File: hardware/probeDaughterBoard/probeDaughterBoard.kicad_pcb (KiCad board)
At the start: 2 copper layers, 45 x 15 mm, 44 parts, among them J1 Conn_02x04_Odd_Even, J2 Conn_01x03_Socket, J3 Conn_01x02_Socket, J4 Conn_01x06

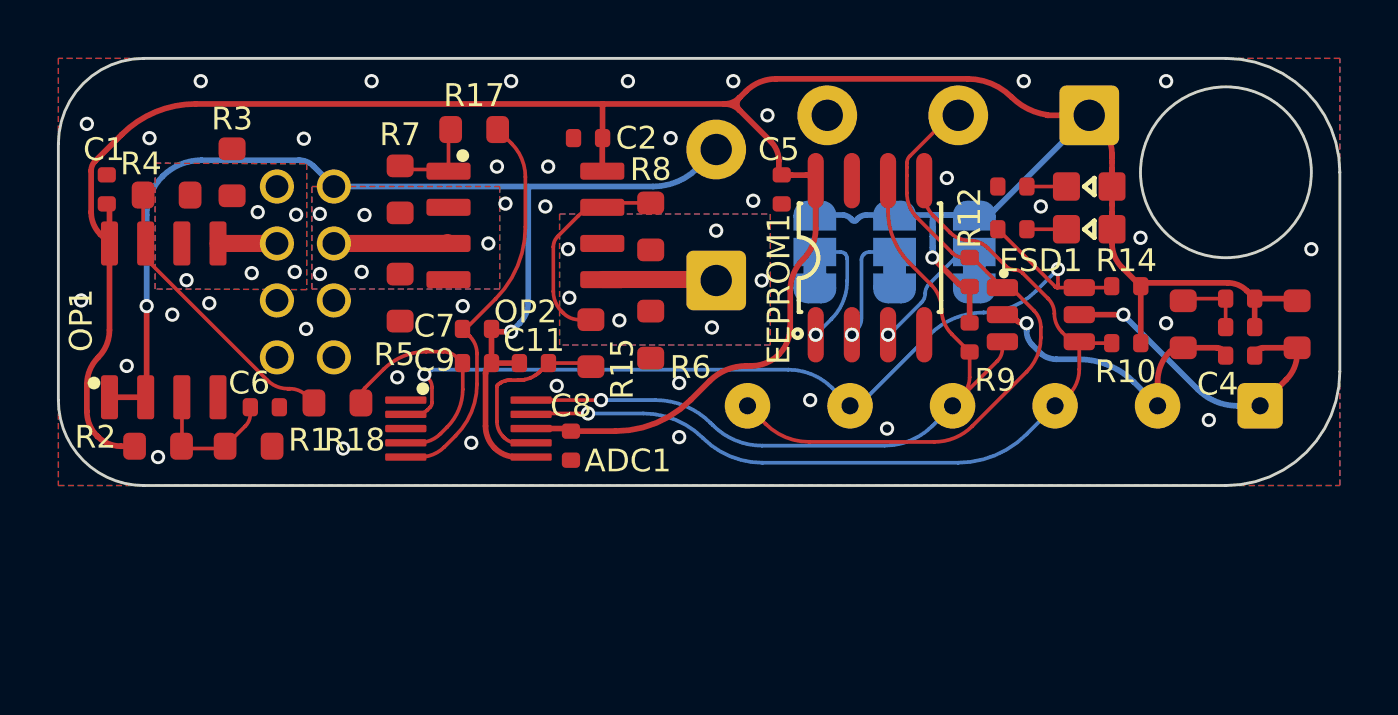
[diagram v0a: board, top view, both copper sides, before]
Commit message: -added CAD models -moved to KiCAD 8.0 -clang formatting -rebuild sensor calibration -add logging and analytics file -added adaptive backlight -added work hours for gps sync
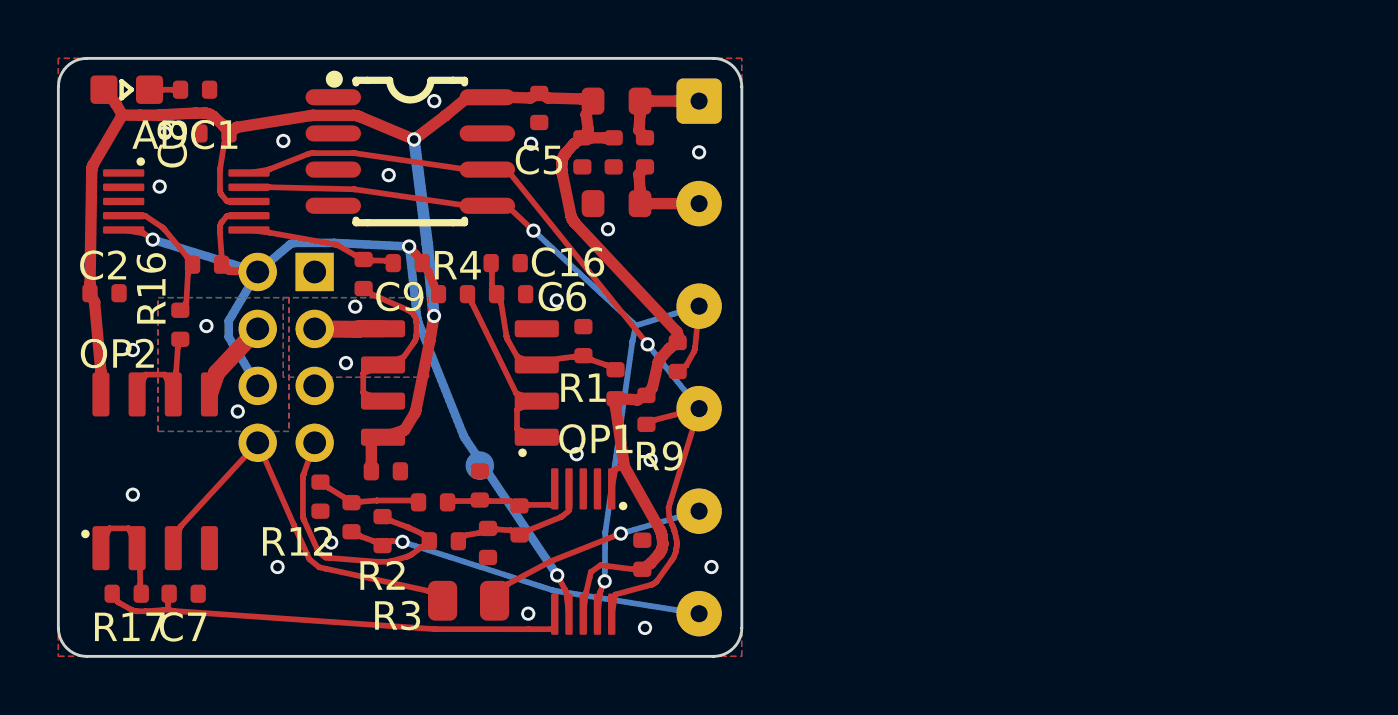
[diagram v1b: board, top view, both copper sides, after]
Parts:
- removed ESD1: SRV05, footprint:SOT-23-6_L2.9-W1.6-P0.95-LS2.8-BR
- removed J2: Conn_01x03_Socket, Connector_Wire:SolderWire-0.5sqmm_1x03_P4.6mm_D0.9mm_OD2.1mm
- removed J3: Conn_01x02_Socket, Connector_Wire:SolderWire-0.5sqmm_1x02_P4.6mm_D0.9mm_OD2.1mm
- removed JP1, JP2, JP3: SolderJumper_3_Bridged12, Jumper:SolderJumper-3_P1.3mm_Bridged12_RoundedPad1.0x1.5mm_NumberLabels
- removed LED2: 0603,Green, footprint:LED0603
- removed R18: 0603,100, footprint:0603_1608Metric
- removed R7, R8: 22k, footprint:0603_1608Metric
- added ADC2: ADS1015, footprint:MSOP-10_L3.0-W3.0-P0.50-LS5.0-BL, F.Cu at (18.4, 17.3)
- added C12: 0402,100nF,16V,X7R, footprint:0402_1005Metric, F.Cu at (20.5, 17.4)
- added C13: 0402,220nF,16V,X7R, footprint:0402_1005Metric, F.Cu at (16.2, 16.2)
- added C14: 0402,22nF,50V,X7R, footprint:0402_1005Metric, F.Cu at (14.8, 15.0)
- added C15: 0402,22nF,50V,X7R, footprint:0402_1005Metric, F.Cu at (15.1, 17.0)
- added C16: 0402,1uF,25V,X5R, footprint:0402_1005Metric, F.Cu at (15.7, 7.19)
- added R16: 0402,100, footprint:0402_1005Metric, F.Cu at (4.28, 9.35)
- added REF**: VREF, footprint:TestPoint_Pad_D1.0mm, B.Cu at (14.8, 14.3)
- R1: value 22k -> 0402,2.2k; footprint footprint:0603_1608Metric -> footprint:0402_1005Metric
- R12: value 0402,2.2k -> 0402,10k
- R13: value 0402,10k -> 0402,100
- R14: value 0402,4.7k -> 0402,100
- R15, R17: value 0603,100 -> 0402,100; footprint footprint:0603_1608Metric -> footprint:0402_1005Metric
- R2: value 22k -> 0402,10k; footprint footprint:0603_1608Metric -> footprint:0402_1005Metric
- R3: value 10k -> 0805,470k; footprint footprint:0603_1608Metric -> footprint:0805_2012Metric
- R4: value 22k -> 0402,100; footprint footprint:0603_1608Metric -> footprint:0402_1005Metric
- R5: value 10k -> 0402,47k; footprint footprint:0603_1608Metric -> footprint:0402_1005Metric
- R6: value 10k -> 0402,12k; footprint footprint:0603_1608Metric -> footprint:0402_1005Metric
- moved LED1 34.0 mm to (2.40, 1.10), turned to 180 degrees
- moved R11 25.9 mm to (10.3, 16.1), turned to 90 degrees
- moved R14 25.6 mm to (13.5, 17.0), turned to 0 degrees
- moved FB1 25.2 mm to (19.6, 1.50), turned to 0 degrees
- moved R12 24.1 mm to (9.20, 15.4), turned to -90 degrees
- moved C3 23.9 mm to (18.4, 3.30), turned to -90 degrees
- moved C10 22.6 mm to (19.5, 3.30), turned to -90 degrees
- moved R13 22.5 mm to (13.2, 15.6), turned to 0 degrees
- moved J4 22.4 mm to (22.5, 1.50), turned to -90 degrees
- moved C4 22.1 mm to (20.6, 3.30), turned to -90 degrees
- moved R17 20.4 mm to (2.40, 18.8)
- moved FB2 20.3 mm to (19.6, 5.10), turned to 0 degrees
- moved C2 17.8 mm to (1.62, 8.25), turned to 0 degrees
- moved R3 17.2 mm to (14.4, 19.0), turned to 180 degrees
- moved C8 16.6 mm to (5.48, 2.64), turned to 180 degrees
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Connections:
- ADC1 pad 1: unconnected-(ADC1-ADDR-Pad1) -> GND
- ADC1 pad 2: /INT -> unconnected-(ADC1-INT-Pad2)
- ADC1 pad 4: /PH_OUT -> /ORP_OUT
- ADC1 pad 5: /ORP_OUT -> /VREF
- ADC1 pad 6: /VREF -> /PH_OUT
- ADC1 pad 7: /NITRATE_OUT -> /VREF
- C11 pad 1: /NITRATE_OUT -> /ORP_OUT
- C6 pad 1: Net-(C6-Pad1) -> Net-(C16-Pad1)
- C7 pad 1: /ORP_OUT -> /EC_OUT
- C7 pad 2: /VREF -> GND
- EEPROM1 pad 1: Net-(EEPROM1-A0) -> GND
- EEPROM1 pad 2: Net-(EEPROM1-A1) -> GND
- EEPROM1 pad 3: Net-(EEPROM1-A2) -> GND
- J1 pad 1: /VREF -> unconnected-(J1-Pin_1-Pad1)
- J1 pad 2: unconnected-(J1-Pin_2-Pad2) -> /VREF
- J1 pad 3: /ORP_IN -> /PH_IN
- J1 pad 4: /PH_IN -> /ORP_IN
- J1 pad 5: /EC_INA -> GND
- J1 pad 6: /TEMP_INB -> /VREF
- J1 pad 7: /EC_INB -> /TEMP_IN
- J1 pad 8: /TEMP_INA -> /EC_IN
- J4 pad 5: /INT -> /EC_DRIVE
- J4 pad 6: /TEMP_OW -> /TEMP_DRIVE
- OP1 pad 1: /VREF -> Net-(OP1---Pad2)
- OP1 pad 2: /VREF -> Net-(OP1---Pad2)
- OP1 pad 3: Net-(C6-Pad1) -> Net-(C16-Pad1)
- OP1 pad 7: Net-(OP1-Pad7) -> /PH_RING
- OP2 pad 1: Net-(OP2-Pad1) -> Net-(OP2---Pad2)
- OP2 pad 2: /ORP_RING -> Net-(OP2---Pad2)
- OP2 pad 3: /ORP_IN -> /EC_IN
- OP2 pad 5: /NITRATE_IN -> /ORP_IN
- OP2 pad 6: /NITRATE_RING -> /ORP_RING
- OP2 pad 7: Net-(OP2-Pad7) -> /ORP_RING
- R1 pad 1: GND -> Net-(C16-Pad1)
- R1 pad 2: Net-(C6-Pad1) -> GND
- R11 pad 1: Net-(LED1-C) -> /TEMP_DRIVE
- R11 pad 2: GND -> /TEMP_REF
- R12 pad 1: +3.3V -> /TEMP_REF
- R12 pad 2: /TEMP_OW -> GND
- R13 pad 1: Net-(LED2-C) -> /TEMP_REF
- R13 pad 2: /INT -> Net-(ADC2-AIN1)
- R14 pad 1: +3.3V -> /TEMP_IN
- R14 pad 2: /INT -> Net-(ADC2-AIN0)
- R15 pad 1: /NITRATE_OUT -> /PH_RING
- R15 pad 2: Net-(OP2-Pad7) -> /PH_OUT
- R17 pad 1: /ORP_OUT -> Net-(OP2---Pad2)
- R17 pad 2: Net-(OP2-Pad1) -> /EC_OUT
- R2 pad 1: Net-(C6-Pad1) -> /TEMP_DRIVE
- R2 pad 2: +3.3V -> /TEMP_IN
- R3 pad 1: /PH_RING -> /EC_DRIVE
- R3 pad 2: GND -> /EC_IN
- R4 pad 1: /PH_RING -> Net-(OP1---Pad2)
- R4 pad 2: Net-(OP1-Pad7) -> /VREF
- R5 pad 1: /ORP_RING -> Net-(LED1-C)
- R6 pad 1: /NITRATE_RING -> +3.3V
- R6 pad 2: GND -> Net-(C16-Pad1)
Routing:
- net +3.3V: track 106.9 -> 70.9 mm, vias 1 -> 2
- net /INT: track 32.2 -> 0.00 mm, vias 2 -> 0
- net /TEMP_OW: track 23.4 -> 0.00 mm
- net /EC_OUT: track 0.00 -> 16.9 mm
- net /EC_IN: track 0.00 -> 14.3 mm
- net /TEMP_DRIVE: track 0.00 -> 12.7 mm, vias 0 -> 1
- net Net-(OP1-Pad7): track 10.1 -> 0.00 mm
- net /TEMP_IN: track 0.00 -> 10.1 mm
- net /ORP_OUT: track 14.2 -> 4.88 mm
- net /3V3_IN: track 11.5 -> 3.44 mm, vias 1 -> 0
- net /EC_DRIVE: track 0.00 -> 7.96 mm, vias 0 -> 1
- net Net-(OP2-Pad7): track 7.33 -> 0.00 mm
- net Net-(C16-Pad1): track 0.00 -> 7.13 mm
- net /GND_IN: track 10.4 -> 3.44 mm, vias 1 -> 0
- net Net-(OP1---Pad2): track 0.00 -> 6.84 mm
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- removed copper zone on B.Cu, net /NITRATE_RING
- removed copper zone on F.Cu, net /NITRATE_RING
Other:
- board size 45 x 15 mm -> 24 x 21 mm
- board text added: "EC DRIVE"
- board text added: "TEMP DRIVE"
- board text removed: "1WIRE"
- board text removed: "INT"
- board text removed: "NITRATE"
- board text removed: "SHIELD"
